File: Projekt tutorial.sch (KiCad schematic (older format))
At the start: 50 parts, among them P1 Silnik1, P2 CONN_01X02, P3 Silnik2, P4 Programator, SW1 SWITCH, U1 LM1117, U10 STM32F030K6, U11 KTIR0711S, U2 TB6612, U3 TB6612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

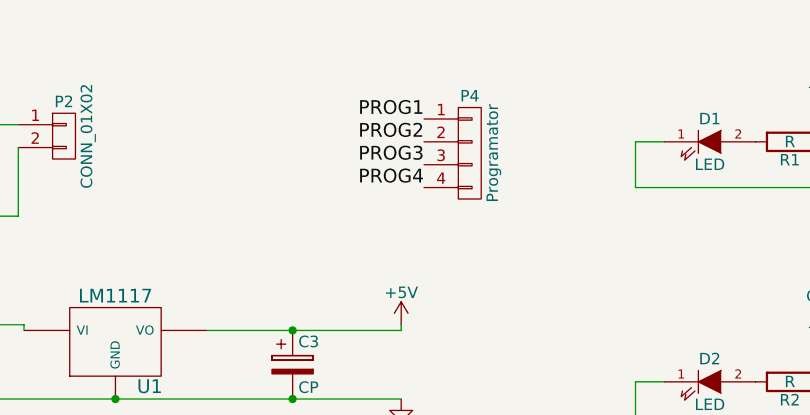
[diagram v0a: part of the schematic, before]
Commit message: Wersja ze złączem micro USB
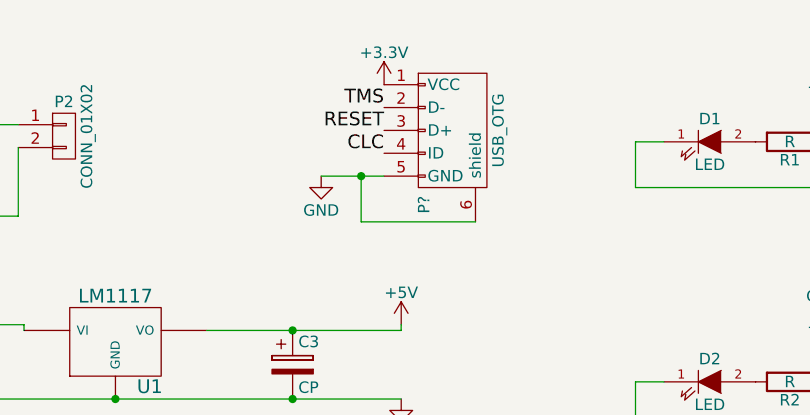
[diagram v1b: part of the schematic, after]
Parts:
- removed P4: Programator, symbol CONN_01X04
- added P?: USB_OTG, symbol USB_OTG
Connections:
- net +3V3: now also P?.1 (VCC)
- net GND: now also P?.5 (GND), P?.6 (shield)
- new net CLC: P?.4 (ID)
- new net RESET: P?.3 (D+)
- new net TMS: P?.2 (D-)
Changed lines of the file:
@@
-PROG4
-$Comp
-L CONN_01X04 P4
-U 1 1 58322D43
-P 3800 1050
-F 0 "P4" H 3800 1300 50  0000 C CNN
-F 1 "Programator" V 3900 1050 50  0000 C CNN
-F 2 "" H 3800 1050 50  0000 C CNN
-F 3 "" H 3800 1050 50  0000 C CNN
-	1    3800 1050
-	1    0    0    -1
-$EndComp
-Text Label 3600 900  2    60   ~ 0
-PROG1
-Text Label 3600 1000 2    60   ~ 0
-PROG2
-Text Label 3600 1100 2    60   ~ 0
-PROG3
-Text Label 3600 1200 2    60   ~ 0
 PROG4
 $Comp
@@
 	1    0    0    -1
 $EndComp
+$Comp
+L USB_OTG P?
+U 1 1 58362023
+P 3725 950
+F 0 "P?" H 4050 825 50  0000 C CNN
+F 1 "USB_OTG" H 3725 1150 50  0000 C CNN
+F 2 "" V 3675 850 50  0000 C CNN
+F 3 "" V 3675 850 50  0000 C CNN
+	1    3725 950
+	0    1    1    0
+$EndComp
+$Comp
+L +3.3V #PWR?
+U 1 1 5836250E
+P 3425 750
+F 0 "#PWR?" H 3425 600 50  0001 C CNN
+F 1 "+3.3V" H 3425 890 50  0000 C CNN
+F 2 "" H 3425 750 50  0000 C CNN
+F 3 "" H 3425 750 50  0000 C CNN
+	1    3425 750
+	1    0    0    -1
+$EndComp
+Text Label 3425 850  2    60   ~ 0
+TMS
+Text Label 3425 950  2    60   ~ 0
+RESET
+Text Label 3425 1050 2    60   ~ 0
+CLC
+$Comp
+L GND #PWR?
+U 1 1 58362756
+P 3150 1150
+F 0 "#PWR?" H 3150 900 50  0001 C CNN
+F 1 "GND" H 3150 1000 50  0000 C CNN
+F 2 "" H 3150 1150 50  0000 C CNN
+F 3 "" H 3150 1150 50  0000 C CNN
+	1    3150 1150
+	1    0    0    -1
+$EndComp
+Wire Wire Line
+	3150 1150 3425 1150
+Wire Wire Line
+	3825 1350 3325 1350
+Wire Wire Line
+	3325 1350 3325 1150
+Connection ~ 3325 1150
 $EndSCHEMATC
